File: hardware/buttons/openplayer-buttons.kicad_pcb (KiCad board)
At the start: 2 copper layers, 14 x 116.1 mm, 10 parts, among them J1 CARRIER, SW1 POWER, SW2 VOL+, SW3 VOL-, SW4 PREV, SW5 PLAY, SW6 NEXT, SW7 MENU

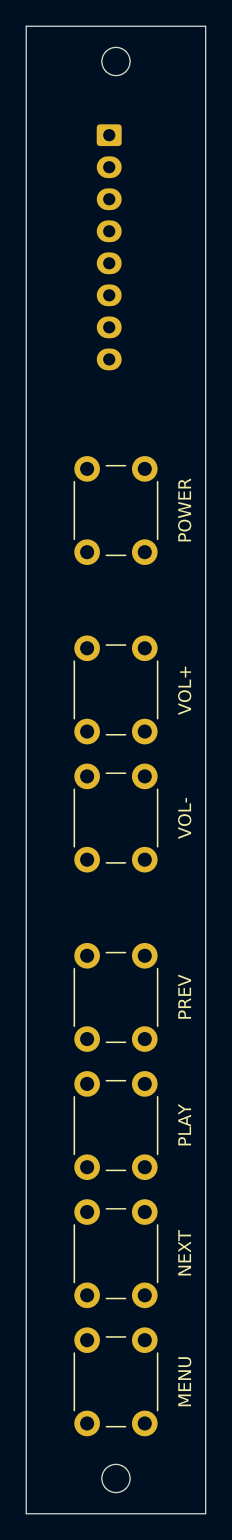
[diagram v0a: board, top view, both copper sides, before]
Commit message: Add routing functionality to build_pcb.py
- Updated the script to include routing for signal tracks.
- Introduced a new constant for signal track width and defined a route order for button nets.
- Implemented a router to handle net routing and GND pour stitching.
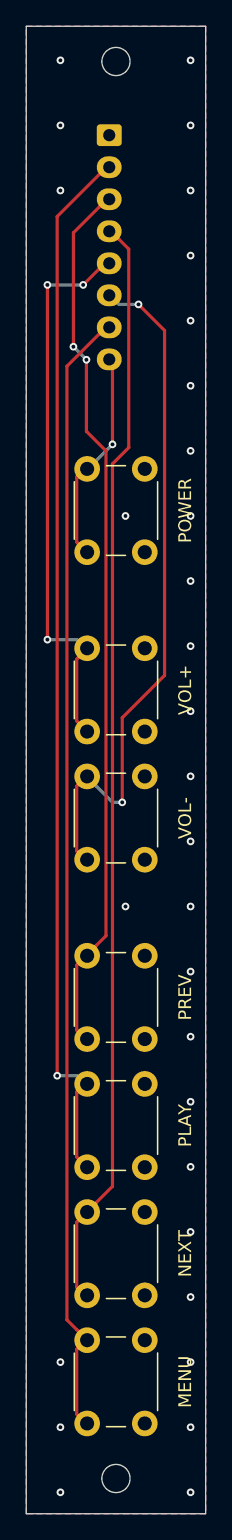
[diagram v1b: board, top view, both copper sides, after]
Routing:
- net /BTN_MENU: track 0.00 -> 88.4 mm
- net /BTN_NEXT: track 0.00 -> 85.8 mm
- net /BTN_PLAY: track 0.00 -> 82.5 mm, vias 0 -> 1
- net /BTN_PREV: track 0.00 -> 69.1 mm, vias 0 -> 2
- net /BTN_VOLDN: track 0.00 -> 54.5 mm, vias 0 -> 2
- net /BTN_VOLUP: track 0.00 -> 43.7 mm, vias 0 -> 3
- net /PWR_KEY: track 0.00 -> 16.7 mm, vias 0 -> 1
- net /GND: vias 0 -> 31
- added copper zone on B.Cu, net /GND
- added copper zone on F.Cu, net /GND
